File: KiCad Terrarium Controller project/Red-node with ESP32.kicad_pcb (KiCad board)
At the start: 2 copper layers, 57.4 x 53.8 mm, 31 parts, among them J1 Moisture Sensor, J2 BMP/BME 280, J3 Motor Battery, J4 Motor, J5 DHT22, J6 Barrel_Jack_Switch, Q1 TIP122, U1 ESP32-DEVKITC-32D

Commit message: Fixed incorrect LED orientation in the schematic
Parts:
- removed G1, G2: LOGO, Libraries:TE_Logo_11.6x4
- removed REF1, REF2, REF3, REF4: MountingHole_2.2mm_M2, MountingHole:MountingHole_2.2mm_M2
- J5: value DHT22 -> DHT22 terminal
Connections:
- D1 pad 1: VCC -> Net-(D1-K)
- D1 pad 2: Net-(D1-Pad2) -> VCC
- D3 pad 1: /GPIO39 -> Net-(D3-K)
- D3 pad 2: Net-(D3-Pad2) -> /GPIO39
- D4 pad 1: /GPIO36 -> Net-(D4-K)
- D4 pad 2: Net-(D4-Pad2) -> /GPIO36
- J1 pad 2: Net-(J1-Pad2) -> unconnected-(J1-Pin_2-Pad2)
- J6 pad 3: Net-(J6-Pad3) -> unconnected-(J6-Pad3)
- R1 pad 1: Net-(D1-Pad2) -> Net-(D1-K)
- R8 pad 1: Net-(D3-Pad2) -> Net-(D3-K)
- R9 pad 1: Net-(D4-Pad2) -> Net-(D4-K)
- U1 pad 10: Net-(U1-Pad10) -> unconnected-(U1-IO26-Pad10)
- U1 pad 11: Net-(U1-Pad11) -> unconnected-(U1-IO27-Pad11)
- U1 pad 12: Net-(U1-Pad12) -> unconnected-(U1-IO14-Pad12)
- U1 pad 13: Net-(U1-Pad13) -> unconnected-(U1-IO12-Pad13)
- U1 pad 15: Net-(U1-Pad15) -> unconnected-(U1-IO13-Pad15)
- U1 pad 16: Net-(U1-Pad16) -> unconnected-(U1-SD2-Pad16)
- U1 pad 17: Net-(U1-Pad17) -> unconnected-(U1-SD3-Pad17)
- U1 pad 18: Net-(U1-Pad18) -> unconnected-(U1-CMD-Pad18)
- U1 pad 2: Net-(U1-Pad2) -> unconnected-(U1-EN-Pad2)
- U1 pad 21: Net-(U1-Pad21) -> unconnected-(U1-IO23-Pad21)
- U1 pad 23: Net-(U1-Pad23) -> unconnected-(U1-TXD0-Pad23)
- U1 pad 24: Net-(U1-Pad24) -> unconnected-(U1-RXD0-Pad24)
- U1 pad 27: Net-(U1-Pad27) -> unconnected-(U1-IO19-Pad27)
- U1 pad 28: Net-(U1-Pad28) -> unconnected-(U1-IO18-Pad28)
- U1 pad 29: Net-(U1-Pad29) -> unconnected-(U1-IO5-Pad29)
- U1 pad 30: Net-(U1-Pad30) -> unconnected-(U1-IO17-Pad30)
- U1 pad 31: Net-(U1-Pad31) -> unconnected-(U1-IO16-Pad31)
- U1 pad 32: Net-(U1-Pad32) -> unconnected-(U1-IO4-Pad32)
- U1 pad 33: Net-(U1-Pad33) -> unconnected-(U1-IO0-Pad33)
- U1 pad 34: Net-(U1-Pad34) -> unconnected-(U1-IO2-Pad34)
- U1 pad 35: Net-(U1-Pad35) -> unconnected-(U1-IO15-Pad35)
- U1 pad 36: Net-(U1-Pad36) -> unconnected-(U1-SD1-Pad36)
- U1 pad 37: Net-(U1-Pad37) -> unconnected-(U1-SD0-Pad37)
- U1 pad 38: Net-(U1-Pad38) -> unconnected-(U1-CLK-Pad38)
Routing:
- net /GPIO39: track 47.9 -> 67.6 mm
- net Net-(D3-Pad2): track 19.7 -> 0.00 mm
- net Net-(D4-Pad2): track 17.2 -> 0.00 mm
- net /GPIO36: track 39.7 -> 56.8 mm
- net VCC: track 95.9 -> 110.0 mm
- net Net-(D1-Pad2): track 14.1 -> 0.00 mm
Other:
- net class Default removed
- net class GND removed
- net class SIGNAL removed
- net class VCC removed
- net class VCC-MOTOR removed

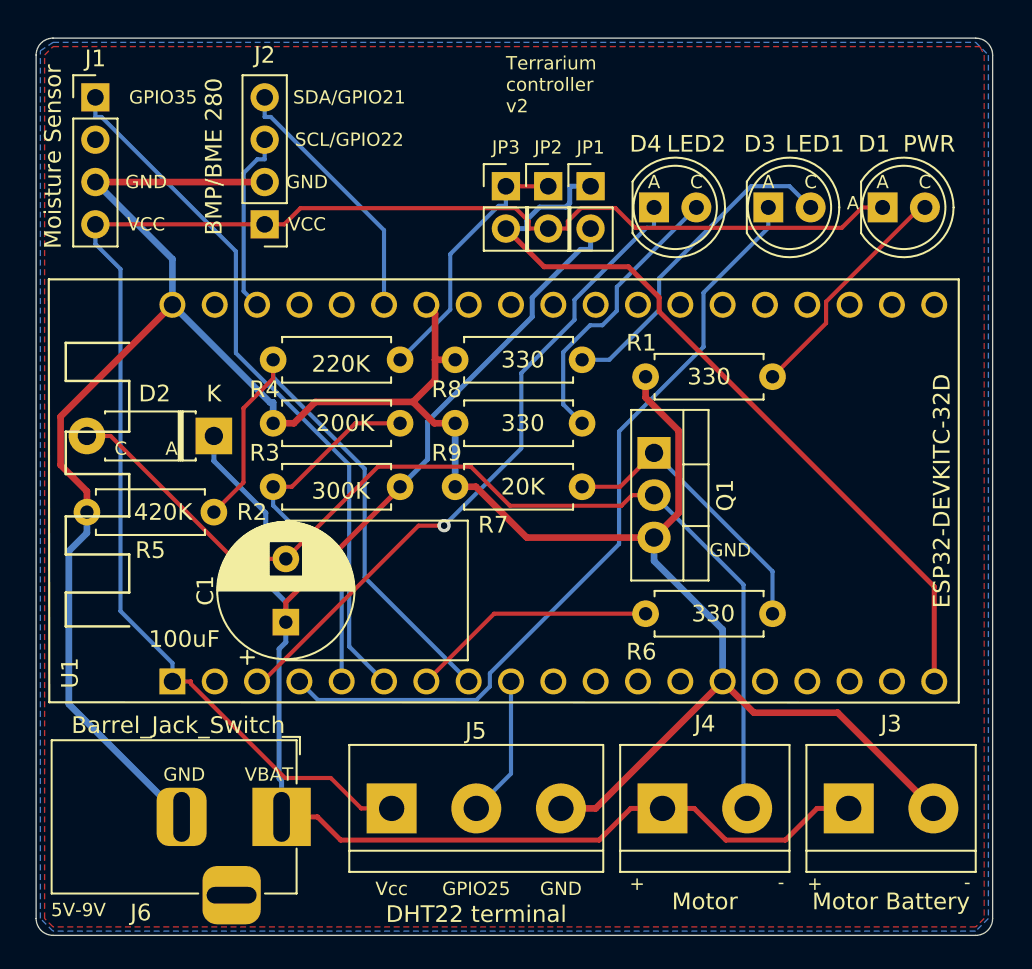
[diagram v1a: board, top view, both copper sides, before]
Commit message: Fixed issues with LED
Both schematic and layouts are fixed.
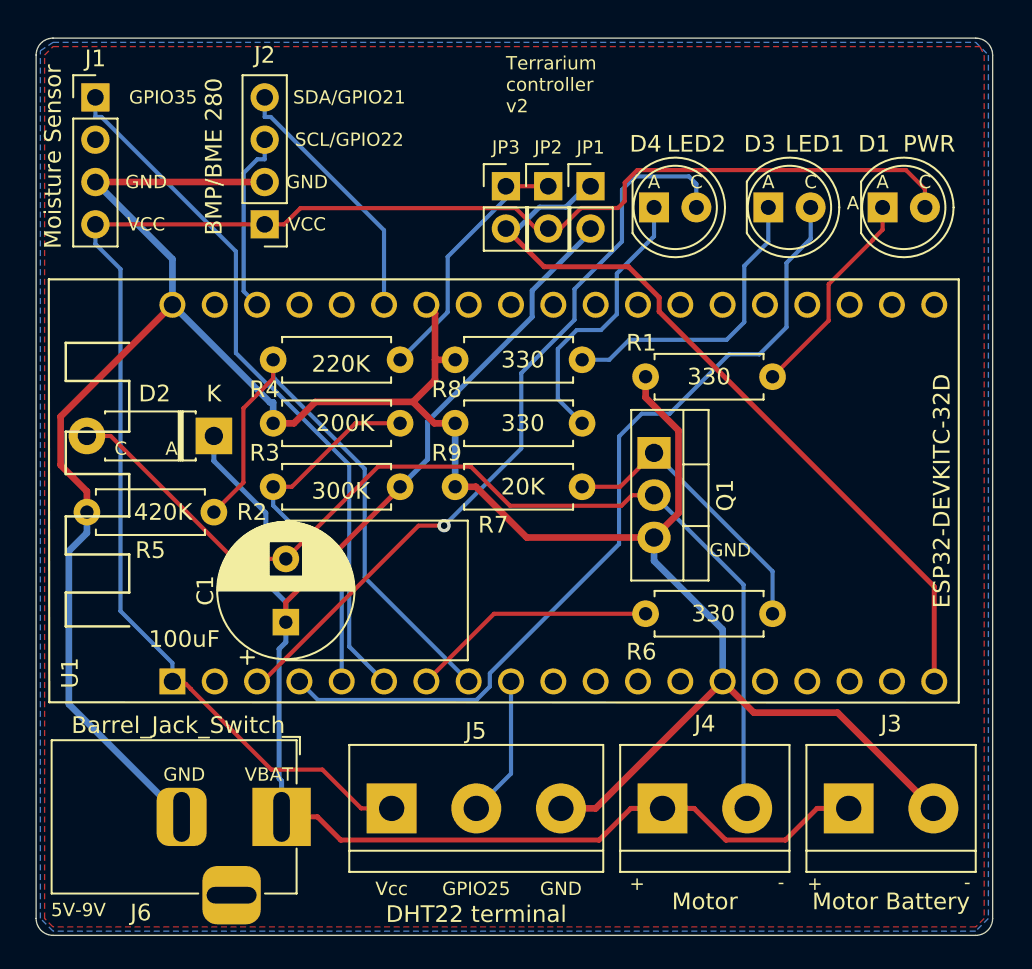
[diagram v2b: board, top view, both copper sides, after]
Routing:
- net Net-(D3-K): track 0.00 -> 18.2 mm
- net Net-(D4-K): track 0.00 -> 16.8 mm
- net /GPIO39: track 67.6 -> 51.0 mm
- net Net-(D1-K): track 0.00 -> 12.9 mm
- net /GPIO36: track 56.8 -> 46.1 mm
- net VCC: track 110.0 -> 100.3 mm
- net /VCC2: track 47.8 -> 46.9 mm
